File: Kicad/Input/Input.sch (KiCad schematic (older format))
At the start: 6 parts

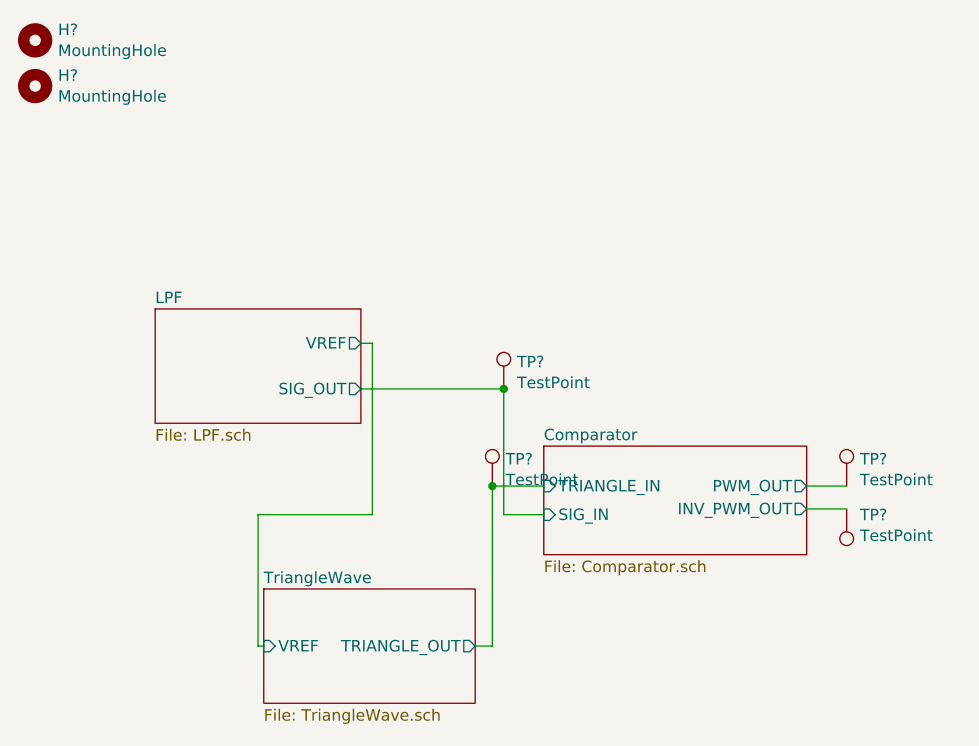
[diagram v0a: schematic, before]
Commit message: Input PCB added
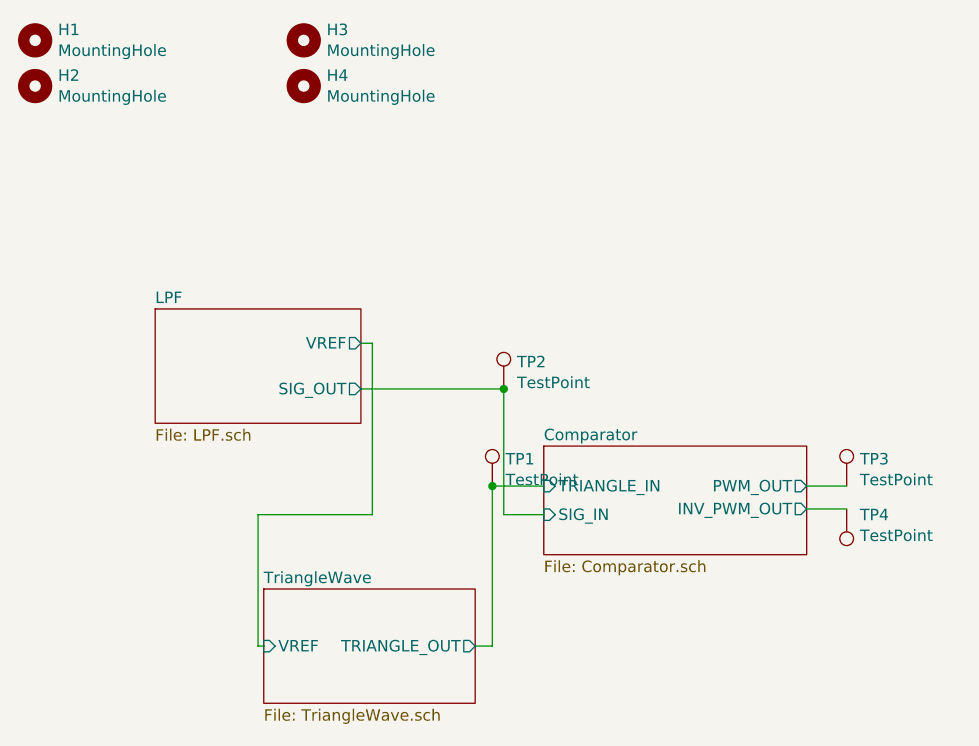
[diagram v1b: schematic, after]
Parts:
- added H3, H4: MountingHole, MountingHole:MountingHole_3.2mm_M3_ISO7380_Pad, symbol Mechanical:MountingHole
- TP1, TP2, TP3, TP4: renamed from TP?; footprint (none) -> TestPoint:TestPoint_Pad_D2.0mm
- gave numbers to parts that had none: 2
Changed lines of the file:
@@
 	7350 3575 7525 3575
 $Comp
-L Connector:TestPoint TP?
+L Connector:TestPoint TP3
 U 1 1 61130EDC
 P 7525 3475
-F 0 "TP?" H 7583 3593 50  0000 L CNN
+F 0 "TP3" H 7583 3593 50  0000 L CNN
 F 1 "TestPoint" H 7583 3502 50  0000 L CNN
-F 2 "" H 7725 3475 50  0001 C CNN
+F 2 "TestPoint:TestPoint_Pad_D2.0mm" H 7725 3475 50  0001 C CNN
 F 3 "~" H 7725 3475 50  0001 C CNN
 	1    7525 3475
@@
 $EndComp
 $Comp
-L Connector:TestPoint TP?
+L Connector:TestPoint TP4
 U 1 1 61131319
 P 7525 3575
-F 0 "TP?" H 7467 3601 50  0000 R CNN
+F 0 "TP4" H 7467 3601 50  0000 R CNN
 F 1 "TestPoint" H 7467 3692 50  0000 R CNN
-F 2 "" H 7725 3575 50  0001 C CNN
+F 2 "TestPoint:TestPoint_Pad_D2.0mm" H 7725 3575 50  0001 C CNN
 F 3 "~" H 7725 3575 50  0001 C CNN
 	1    7525 3575
@@
 $EndComp
 $Comp
-L Connector:TestPoint TP?
+L Connector:TestPoint TP1
 U 1 1 6113172F
 P 5975 3475
-F 0 "TP?" H 6033 3593 50  0000 L CNN
+F 0 "TP1" H 6033 3593 50  0000 L CNN
 F 1 "TestPoint" H 6033 3502 50  0000 L CNN
-F 2 "" H 6175 3475 50  0001 C CNN
+F 2 "TestPoint:TestPoint_Pad_D2.0mm" H 6175 3475 50  0001 C CNN
 F 3 "~" H 6175 3475 50  0001 C CNN
 	1    5975 3475
@@
 Connection ~ 5975 3475
 $Comp
-L Connector:TestPoint TP?
+L Connector:TestPoint TP2
 U 1 1 61131DED
 P 6025 3050
-F 0 "TP?" H 6083 3168 50  0000 L CNN
+F 0 "TP2" H 6083 3168 50  0000 L CNN
 F 1 "TestPoint" H 6083 3077 50  0000 L CNN
-F 2 "" H 6225 3050 50  0001 C CNN
+F 2 "TestPoint:TestPoint_Pad_D2.0mm" H 6225 3050 50  0001 C CNN
 F 3 "~" H 6225 3050 50  0001 C CNN
 	1    6025 3050
@@
 Connection ~ 6025 3050
 $Comp
-L Mechanical:MountingHole H?
+L Mechanical:MountingHole H1
 U 1 1 611409F9
 P 3975 1525
-F 0 "H?" H 4075 1571 50  0000 L CNN
+F 0 "H1" H 4075 1571 50  0000 L CNN
 F 1 "MountingHole" H 4075 1480 50  0000 L CNN
 F 2 "MountingHole:MountingHole_3.2mm_M3_ISO7380_Pad" H 3975 1525 50  0001 C CNN
@@
 $EndComp
 $Comp
-L Mechanical:MountingHole H?
+L Mechanical:MountingHole H2
 U 1 1 61141A37
 P 3975 1725
-F 0 "H?" H 4075 1771 50  0000 L CNN
+F 0 "H2" H 4075 1771 50  0000 L CNN
 F 1 "MountingHole" H 4075 1680 50  0000 L CNN
 F 2 "MountingHole:MountingHole_3.2mm_M3_ISO7380_Pad" H 3975 1725 50  0001 C CNN
@@
 	1    0    0    -1
 $EndComp
+$Comp
+L Mechanical:MountingHole H3
+U 1 1 611314EB
+P 5150 1525
+F 0 "H3" H 5250 1571 50  0000 L CNN
+F 1 "MountingHole" H 5250 1480 50  0000 L CNN
+F 2 "MountingHole:MountingHole_3.2mm_M3_ISO7380_Pad" H 5150 1525 50  0001 C CNN
+F 3 "~" H 5150 1525 50  0001 C CNN
+	1    5150 1525
+	1    0    0    -1
+$EndComp
+$Comp
+L Mechanical:MountingHole H4
+U 1 1 611314F1
+P 5150 1725
+F 0 "H4" H 5250 1771 50  0000 L CNN
+F 1 "MountingHole" H 5250 1680 50  0000 L CNN
+F 2 "MountingHole:MountingHole_3.2mm_M3_ISO7380_Pad" H 5150 1725 50  0001 C CNN
+F 3 "~" H 5150 1725 50  0001 C CNN
+	1    5150 1725
+	1    0    0    -1
+$EndComp
